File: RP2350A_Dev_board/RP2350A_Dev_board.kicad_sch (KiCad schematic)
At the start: 22 parts, among them P1 USB_C_Plug_USB2.0, SW1 SW_Push, U1 W25Q128JVP, Y1 X322512MSB4SI

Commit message: почти всё, осталось только шелкографию сделать и готово
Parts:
- removed P1: USB_C_Plug_USB2.0, Connector_USB:USB_C_Receptacle_GCT_USB4105-xx-A_16P_TopMnt_Horizontal, symbol Connector:USB_C_Plug_USB2.0
- added C16: 100nF, Capacitor_SMD:C_0603_1608Metric, symbol Device:C
- added C17, C18, C22, C23: 22uF, Capacitor_SMD:C_0402_1005Metric, symbol Device:C
- added C19, C20, C21: 100nF, Capacitor_SMD:C_0402_1005Metric, symbol Device:C
- added D1, D2, D3: LED, LED_SMD:LED_0603_1608Metric, symbol Device:LED
- added DD5: ~, SY8843QWC:SY8843QWC, symbol SY8843QWC:SY8843QWC
- added FL1: DLW21SZ900HQ2L, Inductor_SMD:L_CommonModeChoke_Coilcraft_0805USB, symbol Device:Filter_EMI_CommonMode
- added J1, J2, J4: Conn_02x12_Odd_Even, Connector_Hirose:Hirose_DF11-24DP-2DSA_2x12_P2.00mm_Vertical, symbol Connector_Generic:Conn_02x12_Odd_Even
- added J3: Conn_01x04, Connector_Molex:Molex_KK-254_AE-6410-04A_1x04_P2.54mm_Vertical, symbol Connector_Generic:Conn_01x04
- added J5: USB_C_Receptacle_USB2.0_14P, Connector_USB:USB_C_Receptacle_GCT_USB4105-xx-A_16P_TopMnt_Horizontal, symbol Connector:USB_C_Receptacle_USB2.0_14P
- added L4: 0.68uH, Inductor_SMD:L_Cenker_CKCS4020, symbol Device:L
- added R1, R2: 18R, PCM_Resistor_SMD_AKL:R_01005_0402Metric, symbol Device:R
- added R10, R11, R9: 400R, PCM_Resistor_SMD_AKL:R_01005_0402Metric, symbol Device:R
- added R13: 41К, Resistor_SMD:R_0402_1005Metric, symbol Device:R
- added R14: 9.1K, Resistor_SMD:R_0402_1005Metric, symbol Device:R
- added R3, R4: 5.1K, PCM_Resistor_SMD_AKL:R_01005_0402Metric, symbol Device:R
- added R5: 10K, Resistor_SMD:R_0402_1005Metric, symbol Device:R
- added R6, R7: 100K, PCM_Resistor_SMD_AKL:R_01005_0402Metric, symbol Device:R
- added R8: 2K, PCM_Resistor_SMD_AKL:R_01005_0402Metric, symbol Device:R
- added SW2: SW_Push, Button_Switch_SMD:SW_SPST_PTS810, symbol Switch:SW_Push
- added U2: USBLC6-2SC6, Package_TO_SOT_SMD:SOT-23-6, symbol Power_Protection:USBLC6-2SC6
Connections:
- net +3V3: now also U1.8 (VCC), C16.2, C18.1, C19.1, C22.1, DD5.2 (OUT), J4.14 (Pin_14), J4.16 (Pin_16), J4.18 (Pin_18), J4.20 (Pin_20), J4.22 (Pin_22), J4.24 (Pin_24), L4.2, R10.1, R13.2, R6.2, R7.2; no longer DD1.63 (VREG_LX), L1.1
- net Earth: now also SW1.2, U1.4 (GND), U1.9 (EP), C16.1, C17.2, C18.2, C19.2, C20.2, C21.2, C22.2, C23.2, D1.1 (K), D2.1 (K), D3.1 (K), DD5.7 (GND), J3.2 (Pin_2), J4.1 (Pin_1), J4.11 (Pin_11), J4.13 (Pin_13), J4.15 (Pin_15), J4.17 (Pin_17), J4.19 (Pin_19), J4.21 (Pin_21), J4.23 (Pin_23), J4.3 (Pin_3), J4.5 (Pin_5), J4.7 (Pin_7), J4.9 (Pin_9), J5.A1 (GND), J5.A12 (GND), J5.B1 (GND), J5.B12 (GND), J5.S1 (SHIELD), R14.1, R3.1, R4.1, SW2.2, U2.2 (GND); no longer C1.2, C3.2, C4.2, DD1.10 (DVDD_1), DD1.32 (DVDD_2), DD1.51 (DVDD_3), DD1.65 (VREG_FB), L1.2
- net RUN: now reaches SW1.1
- net RUN: now also DD1.35 (RUN), R6.1
- net QSPI_SS: now reaches U1.1 (~{CS})
- net QSPI_SS: now also DD1.75 (QSPI_SS), R7.1, R8.1
- net QSPI_SD1: now reaches U1.2 (DO/IO_{1})
- net QSPI_SD1: now also DD1.74 (QSPI_SD1)
- net QSPI_SD2: now reaches U1.3 (~{WP}/IO_{2})
- net QSPI_SD2: now also DD1.73 (QSPI_SD2)
- net QSPI_SD0: now reaches U1.5 (DI/IO_{0})
- net QSPI_SD0: now also DD1.72 (QSPI_SD0)
- net QSPI_CLK: now reaches U1.6 (CLK)
- net QSPI_CLK: now also DD1.71 (QSPI_SCLK)
- net QSPI_SD3: now reaches U1.7 (~{HOLD}/~{RESET}/IO_{3})
- net QSPI_SD3: now also DD1.70 (QSPI_SD3)
- net IO4: now reaches DD1.1 (GPIO4)
- net IO4: now also J1.5 (Pin_5)
- net IO12: now reaches DD1.11 (GPIO12)
- net IO12: now also J1.13 (Pin_13)
- net IO13: now reaches DD1.12 (GPIO13)
- net IO13: now also J1.14 (Pin_14)
- net IO14: now reaches DD1.13 (GPIO14)
- net IO14: now also J1.15 (Pin_15)
- net IO15: now reaches DD1.14 (GPIO15)
- net IO15: now also J1.16 (Pin_16)
- net IO16: now reaches DD1.16 (GPIO16)
- net IO16: now also J1.17 (Pin_17)
- net IO17: now reaches DD1.17 (GPIO17)
- net IO17: now also J1.18 (Pin_18)
- net IO18: now reaches DD1.18 (GPIO18)
- net IO18: now also J1.19 (Pin_19)
- net IO19: now reaches DD1.19 (GPIO19)
- net IO19: now also J1.20 (Pin_20)
- net IO5: now reaches DD1.2 (GPIO5)
- net IO5: now also J1.6 (Pin_6)
- net IO20: now reaches DD1.20 (GPIO20)
- net IO20: now also J1.21 (Pin_21)
- net IO21: now reaches DD1.21 (GPIO21)
- net IO21: now also J1.22 (Pin_22)
- net IO22: now reaches DD1.22 (GPIO22)
- net IO22: now also J1.23 (Pin_23)
- net IO23: now reaches DD1.23 (GPIO23)
- net IO23: now also J1.24 (Pin_24)
- net IO24: now reaches DD1.25 (GPIO24)
- net IO24: now also J2.1 (Pin_1)
- net IO25: now reaches DD1.26 (GPIO25)
- net IO25: now also J2.2 (Pin_2)
- net IO26: now reaches DD1.27 (GPIO26)
- net IO26: now also J2.3 (Pin_3)
- net IO27: now reaches DD1.28 (GPIO27)
- net IO27: now also J2.4 (Pin_4)
- net IO6: now reaches DD1.3 (GPIO6)
- net IO6: now also J1.7 (Pin_7)
- net SWCLK: now reaches DD1.33 (SWCLK)
- net SWCLK: now also J3.3 (Pin_3)
- net SWDIO: now reaches DD1.34 (SWDIO)
- net SWDIO: now also J3.4 (Pin_4)
- net IO28: now reaches DD1.36 (GPIO28)
- net IO28: now also J2.5 (Pin_5)
- net IO29: now reaches DD1.37 (GPIO29)
- net IO29: now also J2.6 (Pin_6)
- net IO30: now reaches DD1.38 (GPIO30)
- net IO30: now also J2.7 (Pin_7)
- net IO31: now reaches DD1.39 (GPIO31)
- net IO31: now also J2.8 (Pin_8)
- net IO7: now reaches DD1.4 (GPIO7)
- net IO7: now also J1.8 (Pin_8)
- net IO32: now reaches DD1.40 (GPIO32)
- net IO32: now also J2.9 (Pin_9)
- net IO33: now reaches DD1.42 (GPIO33)
- net IO33: now also J2.10 (Pin_10)
- net IO34: now reaches DD1.43 (GPIO34)
- net IO34: now also J2.11 (Pin_11)
- net IO35: now reaches DD1.44 (GPIO35)
- net IO35: now also J2.12 (Pin_12)
- net IO36: now reaches DD1.45 (GPIO36)
- net IO36: now also J2.13 (Pin_13)
- net IO37: now reaches DD1.46 (GPIO37)
- net IO37: now also J2.14 (Pin_14)
- net IO38: now reaches DD1.47 (GPIO38)
- net IO38: now also J2.15 (Pin_15)
- net IO39: now reaches DD1.48 (GPIO39)
- net IO39: now also J2.16 (Pin_16)
- net IO40: now reaches DD1.49 (GPIO40_ADC0)
- net IO40: now also J2.17 (Pin_17)
- net IO41: now reaches DD1.52 (GPIO41_ADC1)
- net IO41: now also J2.18 (Pin_18)
- net IO42: now reaches DD1.53 (GPIO42_ADC2)
- net IO42: now also J2.19 (Pin_19)
- net IO43: now reaches DD1.54 (GPIO43_ADC3)
- net IO43: now also J2.20 (Pin_20)
- net IO44: now reaches DD1.55 (GPIO44_ADC4)
- net IO44: now also J2.21 (Pin_21)
- net IO45: now reaches DD1.56 (GPIO45_ADC5)
- net IO45: now also J2.22 (Pin_22)
- net IO46: now reaches DD1.57 (GPIO46_ADC6)
- net IO46: now also J2.23 (Pin_23)
- net IO47: now reaches DD1.58 (GPIO47_ADC7)
- net IO47: now also J2.24 (Pin_24)
- net IO8: now reaches DD1.6 (GPIO8)
- net IO8: now also J1.9 (Pin_9)
- net USB_mcu-: now reaches DD1.66 (USB_DM)
- net USB_mcu-: now also FL1.3
- net USB_mcu+: now reaches DD1.67 (USB_DP)
- net USB_mcu+: now also FL1.1
- net IO9: now reaches DD1.7 (GPIO9)
- net IO9: now also J1.10 (Pin_10), R11.1
- net IO0: now reaches DD1.77 (GPIO0)
- net IO0: now also J1.1 (Pin_1)
- net IO1: now reaches DD1.78 (GPIO1)
- net IO1: now also J1.2 (Pin_2)
- net IO2: now reaches DD1.79 (GPIO2)
- net IO2: now also J1.3 (Pin_3)
- net IO10: now reaches DD1.8 (GPIO10)
- net IO10: now also J1.11 (Pin_11)
- net IO3: now reaches DD1.80 (GPIO3)
- net IO3: now also J1.4 (Pin_4)
- net IO11: now reaches DD1.9 (GPIO11)
- net IO11: now also J1.12 (Pin_12)
- new net: C1.2, C3.2, C4.2, DD1.10 (DVDD_1), DD1.32 (DVDD_2), DD1.51 (DVDD_3), DD1.65 (VREG_FB), L1.2
- new net: DD1.63 (VREG_LX), L1.1
- new net: D2.2 (A), R10.2
- new net: DD5.1 (FB), R13.1, R14.2
- new net: D3.2 (A), R11.2
- new net: D1.2 (A), R9.2
- new net: R8.2, SW2.1
- new net: DD5.4 (EN), R5.1
- new net: DD5.6 (LX), L4.1
- new net: J5.B5 (CC2), R3.2
- new net: J5.A5 (CC1), R4.2
- new net USB_con+: J5.A6 (D+), J5.B6 (D+), R1.2
- new net USB_con-: J5.A7 (D-), J5.B7 (D-), R2.2
- new net USB_filter+: FL1.2, U2.1 (I/O1)
- new net USB_filter-: FL1.4, U2.3 (I/O2)
- new net USB_res+: R1.1, U2.6 (I/O1)
- new net USB_res-: R2.1, U2.4 (I/O2)
- new net VCC-5V: C17.1, C20.1, C21.1, C23.1, DD5.5 (IN), J3.1 (Pin_1), J4.10 (Pin_10), J4.12 (Pin_12), J4.2 (Pin_2), J4.4 (Pin_4), J4.6 (Pin_6), J4.8 (Pin_8), J5.A4 (VBUS), J5.A9 (VBUS), J5.B4 (VBUS), J5.B9 (VBUS), R5.2, R9.1, U2.5 (VBUS)
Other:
- note added: "3.3V"
- note added: "3.3В 3А"
- note added: "BOOT"
- note added: "DEBUG"
- note added: "FLASH"
- note added: "MCU"
- note added: "RST"
- note added: "USB"
- moved on the sheet: C1, C10, C11, C12, C13, C14, C15, C2, C3, C4, C5, C6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

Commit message: Закончил :)
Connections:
- net Earth: no longer DD1.62 (VREG_PGND)
- net USB_con+: no longer J5.A6 (D+)
- net USB_con-: no longer J5.B7 (D-)
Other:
- moved on the sheet: C1, C10, C11, C12, C13, C14, C15, C16, C2, C20, C21, C23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

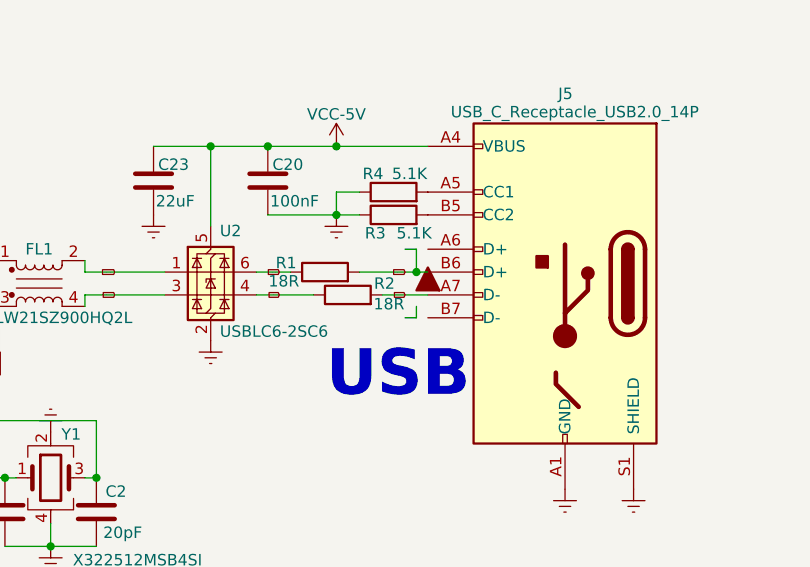
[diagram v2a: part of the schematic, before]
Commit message: Исправил сдвиг внутреннего соединения USB линии
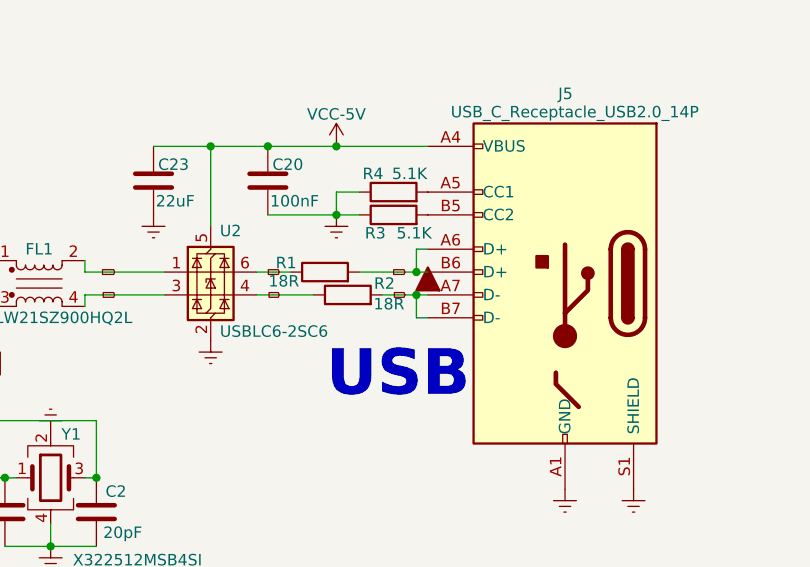
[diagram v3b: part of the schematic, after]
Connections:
- net USB_con+: now also J5.A6 (D+)
- net USB_con-: now also J5.B7 (D-)
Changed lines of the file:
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@@
+	)
+	(junction
+		(at 200.66 127)
+		(diameter 0)
+		(color 0 0 0 0)
 	)
 	(junction
@@
 	(wire
 		(pts
+			(xy 200.66 127) (xy 201.93 127)
+		)
+		(stroke
+			(width 0)
+			(type default)
+		)
+	)
+	(wire
+		(pts
 			(xy 146.05 66.04) (xy 142.24 66.04)
 		)
@@
 	(wire
 		(pts
+			(xy 201.93 129.54) (xy 200.66 129.54)
+		)
+		(stroke
+			(width 0)
+			(type default)
+		)
+	)
+	(wire
+		(pts
 			(xy 146.05 93.98) (xy 142.24 93.98)
 		)
@@
 	(wire
 		(pts
-			(xy 200.66 128.27) (xy 200.66 129.54)
-		)
-		(stroke
-			(width 0)
-			(type default)
-		)
-	)
-	(wire
-		(pts
 			(xy 48.26 121.92) (xy 48.26 119.38)
 		)
@@
 	(wire
 		(pts
+			(xy 200.66 127) (xy 200.66 129.54)
+		)
+		(stroke
+			(width 0)
+			(type default)
+		)
+	)
+	(wire
+		(pts
 			(xy 146.05 60.96) (xy 142.24 60.96)
 		)
@@
 	(wire
 		(pts
-			(xy 196.85 127) (xy 201.93 127)
+			(xy 196.85 127) (xy 200.66 127)
 		)
 		(stroke
@@
 	(wire
 		(pts
-			(xy 200.66 121.92) (xy 199.39 121.92)
-		)
-		(stroke
-			(width 0)
-			(type default)
-		)
-	)
-	(wire
-		(pts
 			(xy 200.66 124.46) (xy 201.93 124.46)
 		)
@@
 	(wire
 		(pts
-			(xy 200.66 129.54) (xy 199.39 129.54)
-		)
-		(stroke
-			(width 0)
-			(type default)
-		)
-	)
-	(wire
-		(pts
 			(xy 72.39 53.34) (xy 73.66 53.34)
 		)
@@
 		)
 		(stroke
+			(width 0)
+			(type default)
+		)
+	)
+	(wire
+		(pts
+			(xy 200.66 121.92) (xy 201.93 121.92)
+		)
+		(stroke
